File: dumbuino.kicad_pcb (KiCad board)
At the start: 2 copper layers, 68.6 x 53.3 mm, 8 parts, among them P1 Power, P2 Analog, P3 Digital, P4 Digital, P5 CONN_01X01, P6 CONN_01X01, P7 CONN_01X01, P8 CONN_01X01

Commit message: Defined board properties
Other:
- copper layers 2 -> 4
- net class Default: clearance 0.2 -> 0.127; trace_width 0.25 -> 0.127; via_drill 0.4 -> 0.3
- rule trace_clearance: 0.2 -> 0.127
- rule trace_min: 0.2 -> 0.127
- rule via_min_size: 0.4 -> 0.6

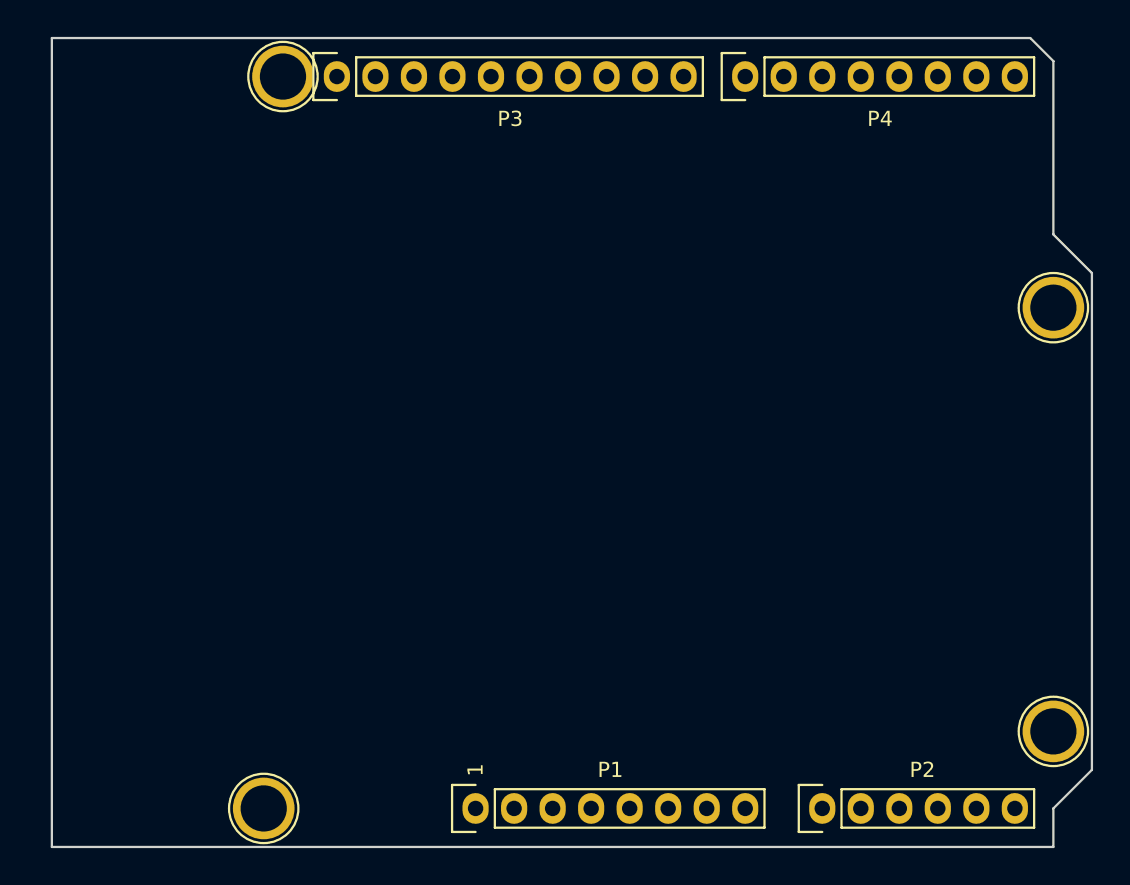
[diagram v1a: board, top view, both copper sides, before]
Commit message: Initial component placement
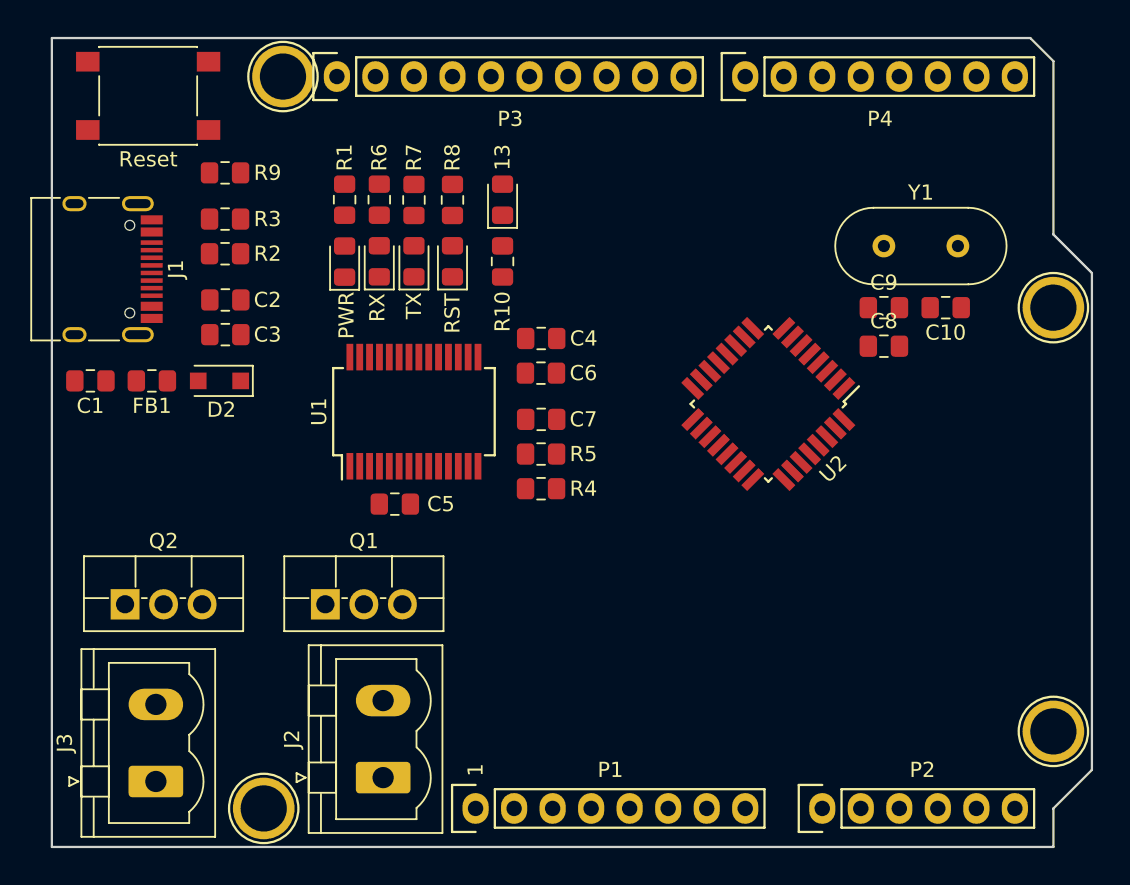
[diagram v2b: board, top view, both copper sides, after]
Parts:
- added 13: 13, LED_SMD:LED_0805_2012Metric_Pad1.15x1.40mm_HandSolder, F.Cu at (140.7, 83.7)
- added C1: 0.01, Capacitor_SMD:C_0805_2012Metric_Pad1.15x1.40mm_HandSolder, F.Cu at (113.5, 95.6)
- added C10: 27p, Capacitor_SMD:C_0805_2012Metric_Pad1.15x1.40mm_HandSolder, F.Cu at (169.9, 90.8)
- added C2: 4u7, Capacitor_SMD:C_0805_2012Metric_Pad1.15x1.40mm_HandSolder, F.Cu at (122.4, 90.3)
- added C3: 0.1, Capacitor_SMD:C_0805_2012Metric_Pad1.15x1.40mm_HandSolder, F.Cu at (122.4, 92.6)
- added C4: 0.1, Capacitor_SMD:C_0805_2012Metric_Pad1.15x1.40mm_HandSolder, F.Cu at (143.3, 92.8)
- added C5: 0.1, Capacitor_SMD:C_0805_2012Metric_Pad1.15x1.40mm_HandSolder, F.Cu at (133.6, 103.8)
- added C6: 0.1, Capacitor_SMD:C_0805_2012Metric_Pad1.15x1.40mm_HandSolder, F.Cu at (143.2, 95.1)
- added C7: 0.1, Capacitor_SMD:C_0805_2012Metric_Pad1.15x1.40mm_HandSolder, F.Cu at (143.3, 98.2)
- added C8: 0.1, Capacitor_SMD:C_0805_2012Metric_Pad1.15x1.40mm_HandSolder, F.Cu at (165.9, 93.3)
- added C9: 27p, Capacitor_SMD:C_0805_2012Metric_Pad1.15x1.40mm_HandSolder, F.Cu at (165.9, 90.8)
- added D2: D_Schottky, Diode_SMD:D_SOD-123F, F.Cu at (122.0, 95.6)
- added FB1: 600, Inductor_SMD:L_0805_2012Metric_Pad1.15x1.40mm_HandSolder, F.Cu at (117.6, 95.6)
- added J1: USB_C_Receptacle_USB2.0, Connector_USB:USB_C_Receptacle_HRO_TYPE-C-31-M-12, F.Cu at (113.5, 88.3)
- added J2: Conn_01x02_Male, Connector_Phoenix_MSTB:PhoenixContact_MSTBVA_2,5_2-G-5,08_1x02_P5.08mm_Vertical, F.Cu at (132.8, 121.8)
- added J3: Conn_01x02_Male, Connector_Phoenix_MSTB:PhoenixContact_MSTBVA_2,5_2-G-5,08_1x02_P5.08mm_Vertical, F.Cu at (117.9, 122.0)
- added PWR: PWR, LED_SMD:LED_0805_2012Metric_Pad1.15x1.40mm_HandSolder, F.Cu at (130.3, 87.8)
- added Q1: Q_NMOS_GDS, Package_TO_SOT_THT:TO-220F-3_Vertical, F.Cu at (129.0, 110.4)
- added Q2: Q_NMOS_GDS, Package_TO_SOT_THT:TO-220F-3_Vertical, F.Cu at (115.8, 110.4)
- added R1: 1k, Resistor_SMD:R_0805_2012Metric_Pad1.15x1.40mm_HandSolder, F.Cu at (130.3, 83.7)
- added R10: 1k, Resistor_SMD:R_0805_2012Metric_Pad1.15x1.40mm_HandSolder, F.Cu at (140.7, 87.8)
- added R2: 5.11k, Resistor_SMD:R_0805_2012Metric_Pad1.15x1.40mm_HandSolder, F.Cu at (122.4, 87.2)
- added R3: 5.11k, Resistor_SMD:R_0805_2012Metric_Pad1.15x1.40mm_HandSolder, F.Cu at (122.4, 85.0)
- added R4: 1K, Resistor_SMD:R_0805_2012Metric_Pad1.15x1.40mm_HandSolder, F.Cu at (143.3, 102.7)
- added R5: 1K, Resistor_SMD:R_0805_2012Metric_Pad1.15x1.40mm_HandSolder, F.Cu at (143.3, 100.5)
- added R6: 1k, Resistor_SMD:R_0805_2012Metric_Pad1.15x1.40mm_HandSolder, F.Cu at (132.6, 83.7)
- added R7: 1k, Resistor_SMD:R_0805_2012Metric_Pad1.15x1.40mm_HandSolder, F.Cu at (134.9, 83.7)
- added R8: 1k, Resistor_SMD:R_0805_2012Metric_Pad1.15x1.40mm_HandSolder, F.Cu at (137.4, 83.7)
- added R9: 1k, Resistor_SMD:R_0805_2012Metric_Pad1.15x1.40mm_HandSolder, F.Cu at (122.4, 81.9)
- added RST: Reset, LED_SMD:LED_0805_2012Metric_Pad1.15x1.40mm_HandSolder, F.Cu at (137.4, 87.7)
- added RX: RX, LED_SMD:LED_0805_2012Metric_Pad1.15x1.40mm_HandSolder, F.Cu at (132.6, 87.7)
- added Reset: ~Reset, Button_Switch_SMD:SW_SPST_PTS645, F.Cu at (117.3, 76.8)
- added TX: TX, LED_SMD:LED_0805_2012Metric_Pad1.15x1.40mm_HandSolder, F.Cu at (134.9, 87.7)
- added U1: FT232RL, Package_SO:SSOP-28_5.3x10.2mm_P0.65mm, F.Cu at (134.9, 97.7)
- added U2: ATmega328PB-AU, Package_QFP:TQFP-32_7x7mm_P0.8mm, F.Cu at (158.2, 97.2)
- added Y1: 16M, Crystal:Crystal_HC49-U_Vertical, F.Cu at (165.9, 86.7)
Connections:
- P1 pad 1: Net-(P1-Pad1) -> (no net)
- P1 pad 2: /IOREF -> (no net)
- P1 pad 4: +3V3 -> (no net)
- P1 pad 8: /Vin -> (no net)
- P3 pad 3: /AREF -> (no net)
- P5 pad 1: Net-(P5-Pad1) -> (no net)
- P6 pad 1: Net-(P6-Pad1) -> (no net)
- P7 pad 1: Net-(P7-Pad1) -> (no net)
- P8 pad 1: Net-(P8-Pad1) -> (no net)

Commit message: Finished initial board layout
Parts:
- moved U2 5.24 mm to (160.3, 102.0)
- moved C7 5.08 mm to (143.3, 103.3)
- moved C8 4.11 mm to (165.6, 97.4), turned to 135 degrees
- moved R4 4.06 mm to (143.3, 98.7)
- moved Y1 1.83 mm to (164.3, 87.8)
- moved C9 1.63 mm to (164.6, 91.8)
- moved C10 1.27 mm to (169.2, 91.8)
- moved R5 0.51 mm to (143.3, 101.0)
- moved R8 0.25 mm to (137.2, 83.7)
- moved RST 0.25 mm to (137.2, 87.7)
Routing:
- net +5V: track 0.00 -> 120.9 mm
- net /Reset: track 0.00 -> 107.0 mm, vias 0 -> 3
- net /A5(SCL): track 0.00 -> 80.9 mm, vias 0 -> 1
- net /A4(SDA): track 0.00 -> 76.0 mm, vias 0 -> 1
- net /10(**/SS): track 0.00 -> 73.4 mm, vias 0 -> 1
- net /1(Tx): track 0.00 -> 65.3 mm, vias 0 -> 2
- net /0(Rx): track 0.00 -> 64.7 mm, vias 0 -> 2
- net /9(**): track 0.00 -> 59.2 mm, vias 0 -> 1
- net /13(SCK): track 0.00 -> 43.2 mm
- net GND: track 0.00 -> 38.9 mm, vias 0 -> 12
- net /2: track 0.00 -> 34.7 mm
- net /12(MISO): track 0.00 -> 34.3 mm
- net /4: track 0.00 -> 32.4 mm
- net /11(**/MOSI): track 0.00 -> 31.7 mm
- net /3(**): track 0.00 -> 31.6 mm
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- added copper zone on B.Cu, net GND

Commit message: Adjusted tracks
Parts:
- moved J2 20.3 mm to (117.9, 108.1)
- moved Q2 17.7 mm to (132.1, 117.5), turned to 180 degrees
- moved C6 9.09 mm to (134.9, 91.6), turned to 180 degrees
- moved R8 6.59 mm to (130.8, 81.9), turned to 0 degrees
- moved RST 6.27 mm to (134.9, 81.9), turned to 180 degrees
- moved R1 5.11 mm to (130.8, 88.8), turned to 0 degrees
- moved PWR 4.69 mm to (134.9, 88.8), turned to 180 degrees
- moved C4 4.50 mm to (138.9, 91.6)
- moved R7 4.09 mm to (130.8, 84.2), turned to 0 degrees
- moved R10 3.87 mm to (142.2, 84.2), turned to 180 degrees
- moved TX 3.55 mm to (134.9, 84.2), turned to 180 degrees
- moved R6 3.32 mm to (130.8, 86.5), turned to 0 degrees
- moved Q1 3.09 mm to (132.1, 109.9), turned to 180 degrees
- moved RX 2.60 mm to (134.9, 86.5), turned to 180 degrees
- moved 13 2.33 mm to (142.2, 81.9), turned to 180 degrees
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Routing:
- net /10(**/SS): track 73.4 -> 65.2 mm, vias 1 -> 2
- net Net-(D4-Pad1): track 5.42 -> 11.7 mm
- net +5V: track 120.9 -> 115.0 mm
- net Net-(C4-Pad1): track 8.11 -> 2.55 mm
- net /9(**): track 59.2 -> 64.6 mm, vias 1 -> 2
- net /4: track 32.4 -> 35.8 mm
- net Net-(D3-Pad1): track 5.83 -> 8.40 mm
- net /3(**): track 31.6 -> 33.7 mm
- net GND: track 38.9 -> 40.3 mm
- net /13(SCK): track 43.2 -> 41.8 mm
- net /Reset: track 107.0 -> 106.1 mm, vias 3 -> 5
- net Net-(J1-PadA7): track 26.5 -> 27.5 mm
- net /2: track 34.7 -> 35.6 mm
- net Net-(C7-Pad1): track 14.1 -> 13.4 mm
- net Net-(J1-PadA6): track 29.0 -> 29.7 mm
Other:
- board text added: "DIGITAL PWM(~~)"

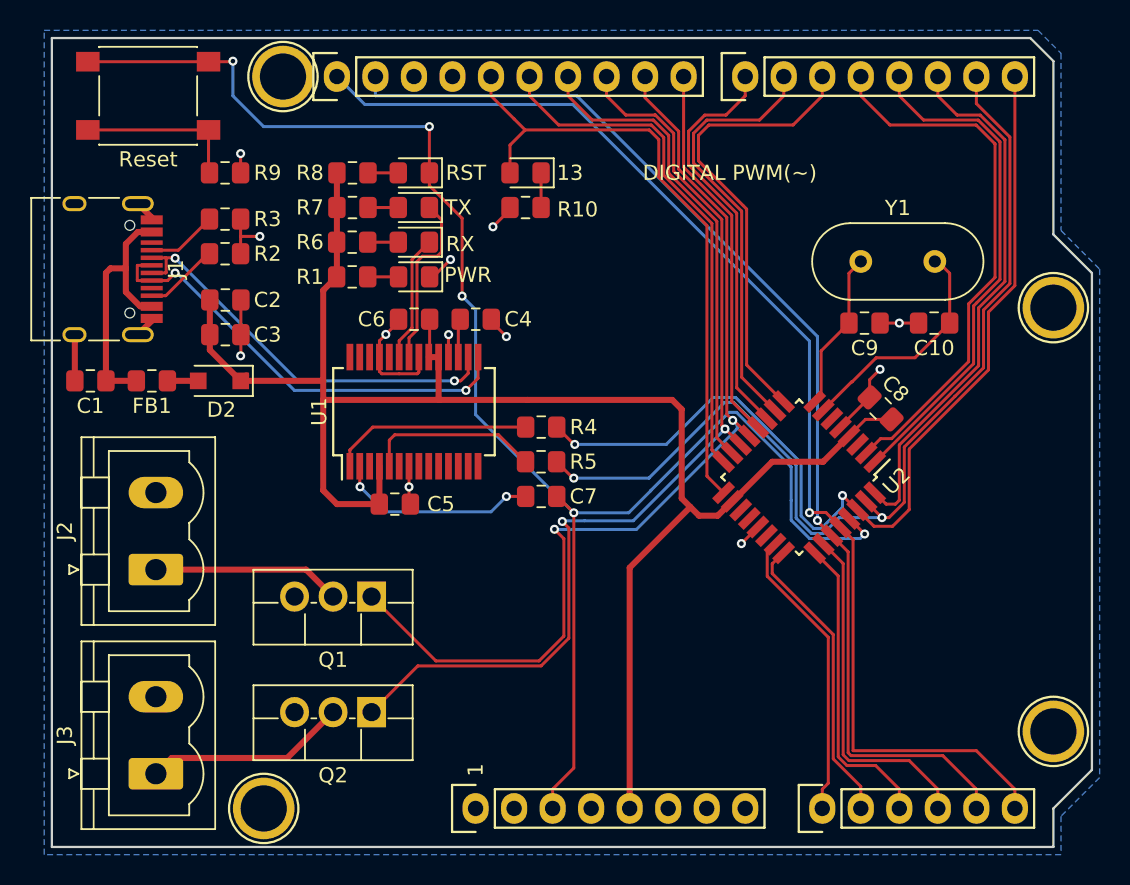
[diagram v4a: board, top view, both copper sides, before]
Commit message: Updated F.SilkS
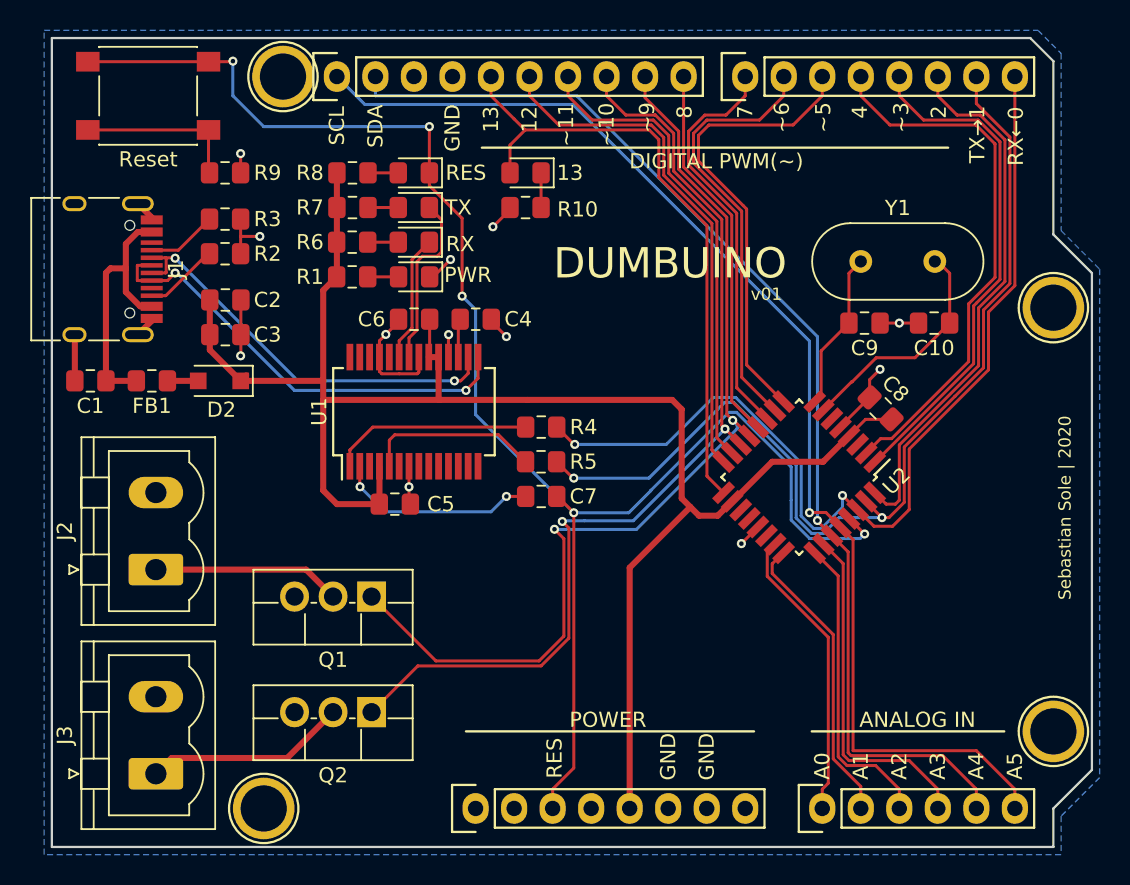
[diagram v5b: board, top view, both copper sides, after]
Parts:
- renumbered RST to RES
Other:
- board text added: "12"
- board text added: "13"
- board text added: "2"
- board text added: "4"
- board text added: "7"
- board text added: "8"
- board text added: "A0"
- board text added: "A1"
- board text added: "A2"
- board text added: "A3"
- board text added: "A4"
- board text added: "A5"
- board text added: "ANALOG IN"
- board text added: "DUMBUINO"
- board text added: "GND"
- board text added: "POWER"
- board text added: "RES"
- board text added: "RX←0"
- board text added: "SCL"
- board text added: "SDA"
- board text added: "Sebastian Sole | 2020"
- board text added: "TX→1"
- board text added: "v01"
- board text added: "~~10"
- board text added: "~~11"
- board text added: "~~3"
- board text added: "~~5"
- board text added: "~~6"
- board text added: "~~9"
- board text removed: "1"
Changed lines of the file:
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@@
   (general
     (thickness 1.6002)
-    (drawings 28)
+    (drawings 61)
     (tracks 473)
     (zones 0)
@@
     (tags "LED handsolder")
     (attr smd)
-    (fp_text reference RST (at -3.438 0 180) (layer F.SilkS)
+    (fp_text reference RES (at -3.438 0 180) (layer F.SilkS)
       (effects (font (size 1 1) (thickness 0.15)))
     )
@@
     (pad 1 thru_hole circle (at 0 0) (size 4.064 4.064) (drill 3.048) (layers *.Cu *.Mask F.SilkS))
   )
-  (gr_text "DIGITAL PWM(~~)" (at 155.702 81.915) (layer F.SilkS)
-    (effects (font (size 1 1) (thickness 0.15)))
-  )
-  (gr_text 1 (at 138.938 121.285 90) (layer F.SilkS)
-    (effects (font (size 1 1) (thickness 0.15)))
-  )
+  (gr_text v01 (at 158.115 89.916) (layer F.SilkS)
+    (effects (font (size 0.8128 0.8128) (thickness 0.1524)))
+  )
+  (gr_text "Sebastian Sole | 2020" (at 177.8 97.917 90) (layer F.SilkS)
+    (effects (font (size 0.8128 0.8128) (thickness 0.1524)) (justify right))
+  )
+  (gr_text DUMBUINO (at 151.765 87.884) (layer F.SilkS)
+    (effects (font (size 2 2) (thickness 0.2)))
+  )
+  (gr_line (start 161.1 118.745) (end 173.8 118.745) (layer F.SilkS) (width 0.1524))
+  (gr_line (start 138.3 118.745) (end 157.3 118.745) (layer F.SilkS) (width 0.1524))
+  (gr_text A5 (at 174.498 121.031 90) (layer F.SilkS)
+    (effects (font (size 1 1) (thickness 0.15)))
+  )
+  (gr_text A4 (at 171.958 121.031 90) (layer F.SilkS)
+    (effects (font (size 1 1) (thickness 0.15)))
+  )
+  (gr_text A3 (at 169.418 121.031 90) (layer F.SilkS)
+    (effects (font (size 1 1) (thickness 0.15)))
+  )
+  (gr_text A2 (at 166.878 121.031 90) (layer F.SilkS)
+    (effects (font (size 1 1) (thickness 0.15)))
+  )
+  (gr_text A1 (at 164.338 121.031 90) (layer F.SilkS)
+    (effects (font (size 1 1) (thickness 0.15)))
+  )
+  (gr_text A0 (at 161.798 121.031 90) (layer F.SilkS)
+    (effects (font (size 1 1) (thickness 0.15)))
+  )
+  (gr_text RES (at 144.145 120.507191 90) (layer F.SilkS)
+    (effects (font (size 1 1) (thickness 0.15)))
+  )
+  (gr_text GND (at 154.178 120.411953 90) (layer F.SilkS)
+    (effects (font (size 1 1) (thickness 0.15)))
+  )
+  (gr_text GND (at 151.638 120.411953 90) (layer F.SilkS)
+    (effects (font (size 1 1) (thickness 0.15)))
+  )
+  (gr_text POWER (at 147.664 117.983) (layer F.SilkS)
+    (effects (font (size 1 1) (thickness 0.15)))
+  )
+  (gr_text "ANALOG IN" (at 168.074 117.983) (layer F.SilkS)
+    (effects (font (size 1 1) (thickness 0.15)))
+  )
+  (gr_line (start 139.35 80.254) (end 170.1 80.254) (layer F.SilkS) (width 0.1524))
+  (gr_text RX←0 (at 174.5615 79.501905 90) (layer F.SilkS)
+    (effects (font (size 1 1) (thickness 0.15)))
+  )
+  (gr_text TX→1 (at 172.0215 79.382857 90) (layer F.SilkS)
+    (effects (font (size 1 1) (thickness 0.15)))
+  )
+  (gr_text 2 (at 169.4815 77.906667 90) (layer F.SilkS)
+    (effects (font (size 1 1) (thickness 0.15)))
+  )
+  (gr_text ~~3 (at 167.005 78.26381 90) (layer F.SilkS)
+    (effects (font (size 1 1) (thickness 0.15)))
+  )
+  (gr_text 4 (at 164.2745 77.906667 90) (layer F.SilkS)
+    (effects (font (size 1 1) (thickness 0.15)))
+  )
+  (gr_text ~~5 (at 161.8615 78.26381 90) (layer F.SilkS)
+    (effects (font (size 1 1) (thickness 0.15)))
+  )
+  (gr_text ~~6 (at 159.131 78.26381 90) (layer F.SilkS)
+    (effects (font (size 1 1) (thickness 0.15)))
+  )
+  (gr_text 7 (at 156.718 77.906667 90) (layer F.SilkS)
+    (effects (font (size 1 1) (thickness 0.15)))
+  )
+  (gr_text 8 (at 152.7175 77.906667 90) (layer F.SilkS)
+    (effects (font (size 1 1) (thickness 0.15)))
+  )
+  (gr_text ~~9 (at 150.241 78.26381 90) (layer F.SilkS)
+    (effects (font (size 1 1) (thickness 0.15)))
+  )
+  (gr_text ~~10 (at 147.574 78.74 90) (layer F.SilkS)
+    (effects (font (size 1 1) (thickness 0.15)))
+  )
+  (gr_text ~~11 (at 144.907 78.74 90) (layer F.SilkS)
+    (effects (font (size 1 1) (thickness 0.15)))
+  )
+  (gr_text 12 (at 142.494 78.382857 90) (layer F.SilkS)
+    (effects (font (size 1 1) (thickness 0.15)))
+  )
+  (gr_text 13 (at 139.954 78.382857 90) (layer F.SilkS)
+    (effects (font (size 1 1) (thickness 0.15)))
+  )
+  (gr_text GND (at 137.414 78.954286 90) (layer F.SilkS)
+    (effects (font (size 1 1) (thickness 0.15)))
+  )
+  (gr_text SDA (at 132.334 78.835238 90) (layer F.SilkS)
+    (effects (font (size 1 1) (thickness 0.15)))
+  )
+  (gr_text SCL (at 129.794 78.811429 90) (layer F.SilkS)
+    (effects (font (size 1 1) (thickness 0.15)))
+  )
+  (gr_text "DIGITAL PWM(~~)" (at 154.813 81.153) (layer F.SilkS)
+    (effects (font (size 1 1) (thickness 0.15)))
+  )
